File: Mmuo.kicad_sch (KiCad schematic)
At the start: 103 parts, among them IC1 A121-001-T&R, IC2 BQ24253RGER, IC3 ADPL40502AUJZ-1.8-R7, IC4 RAA2361052GNP#HC5, J1 USB_C_Receptacle_USB2.0_16P, J2 B2B-PH-K-S, J3 SW_Debug, Q1 BSS84, Q2 BSS138, Q3 MMBT3904, SW1 PTS815, U1 USBLC6-2SC6, U3 EKMB1309113K, U4 STM32WB55CGU6, U5 MCP9808_MSOP, Y1 24MHz, Y2 32MHz, Y3 32K768

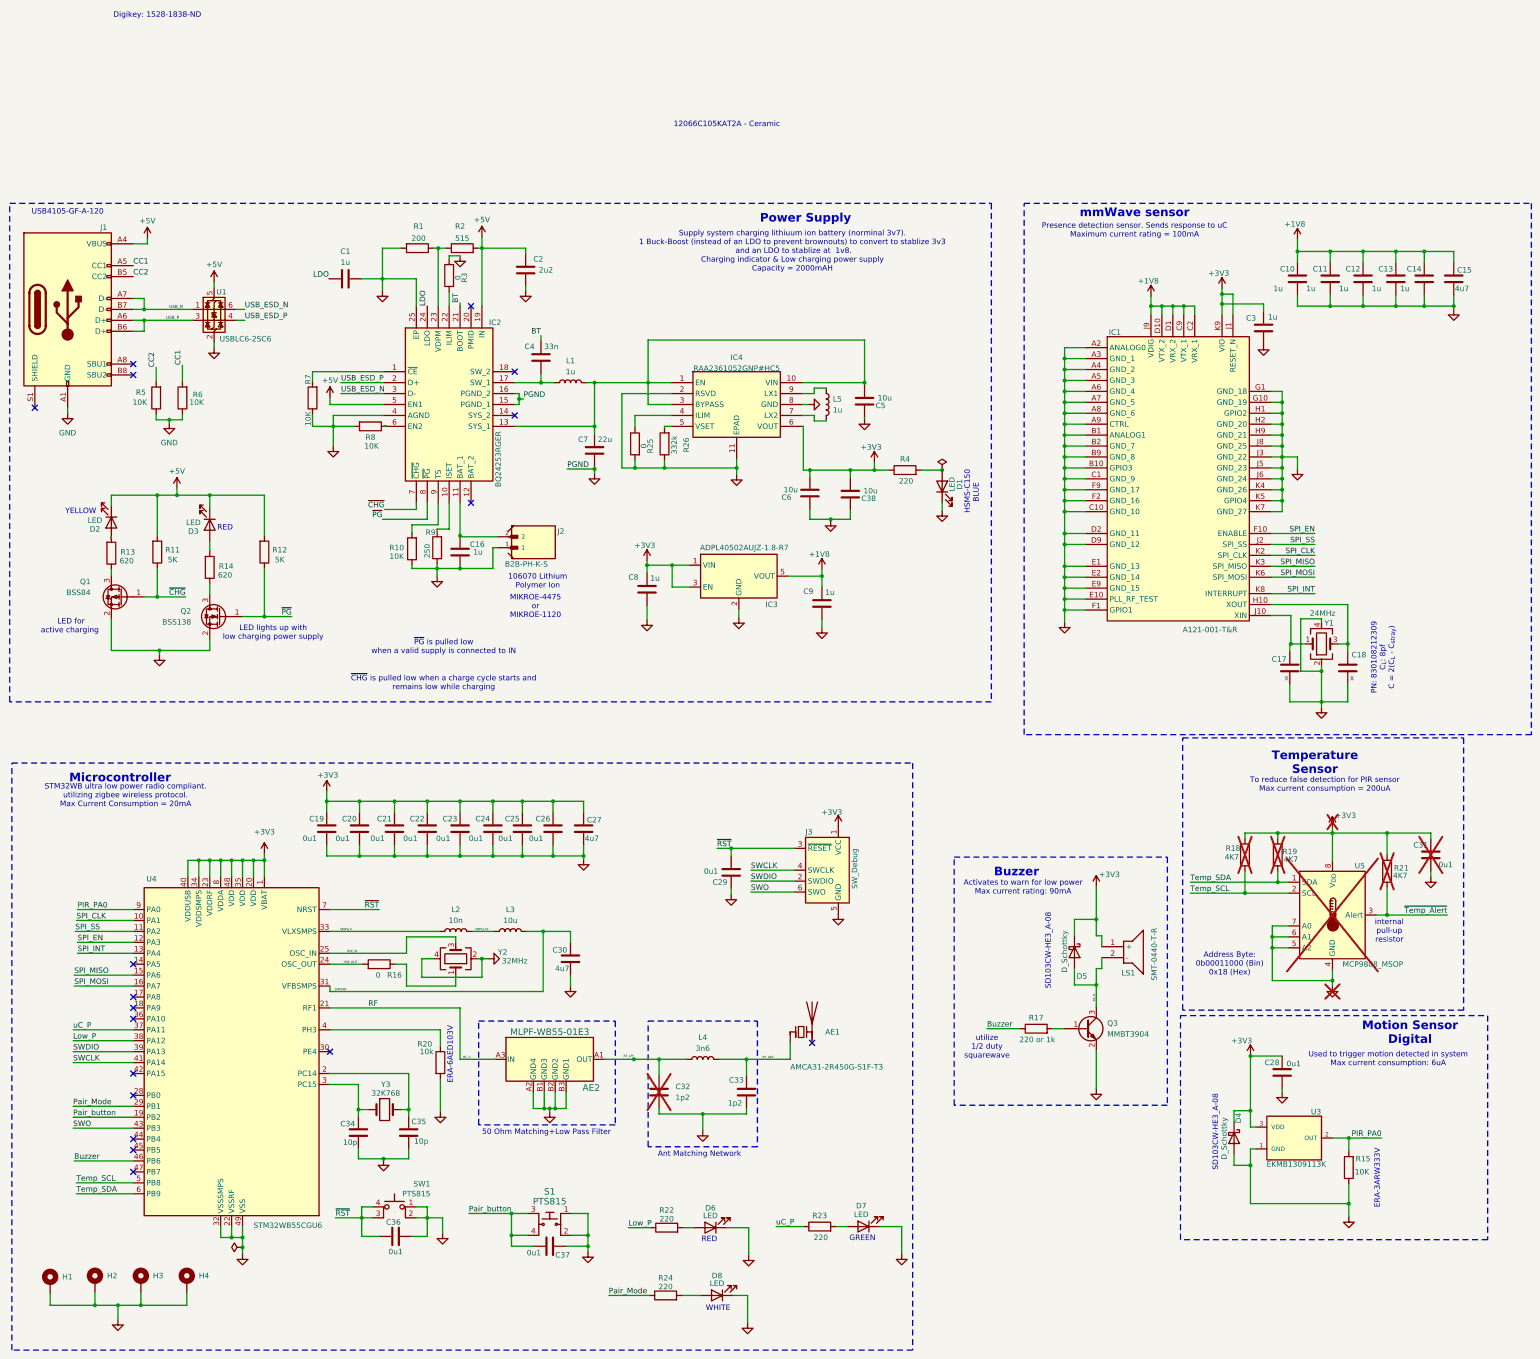
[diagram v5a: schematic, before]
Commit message: V2.0: using a TOF sensor instead of a mmWave sensor
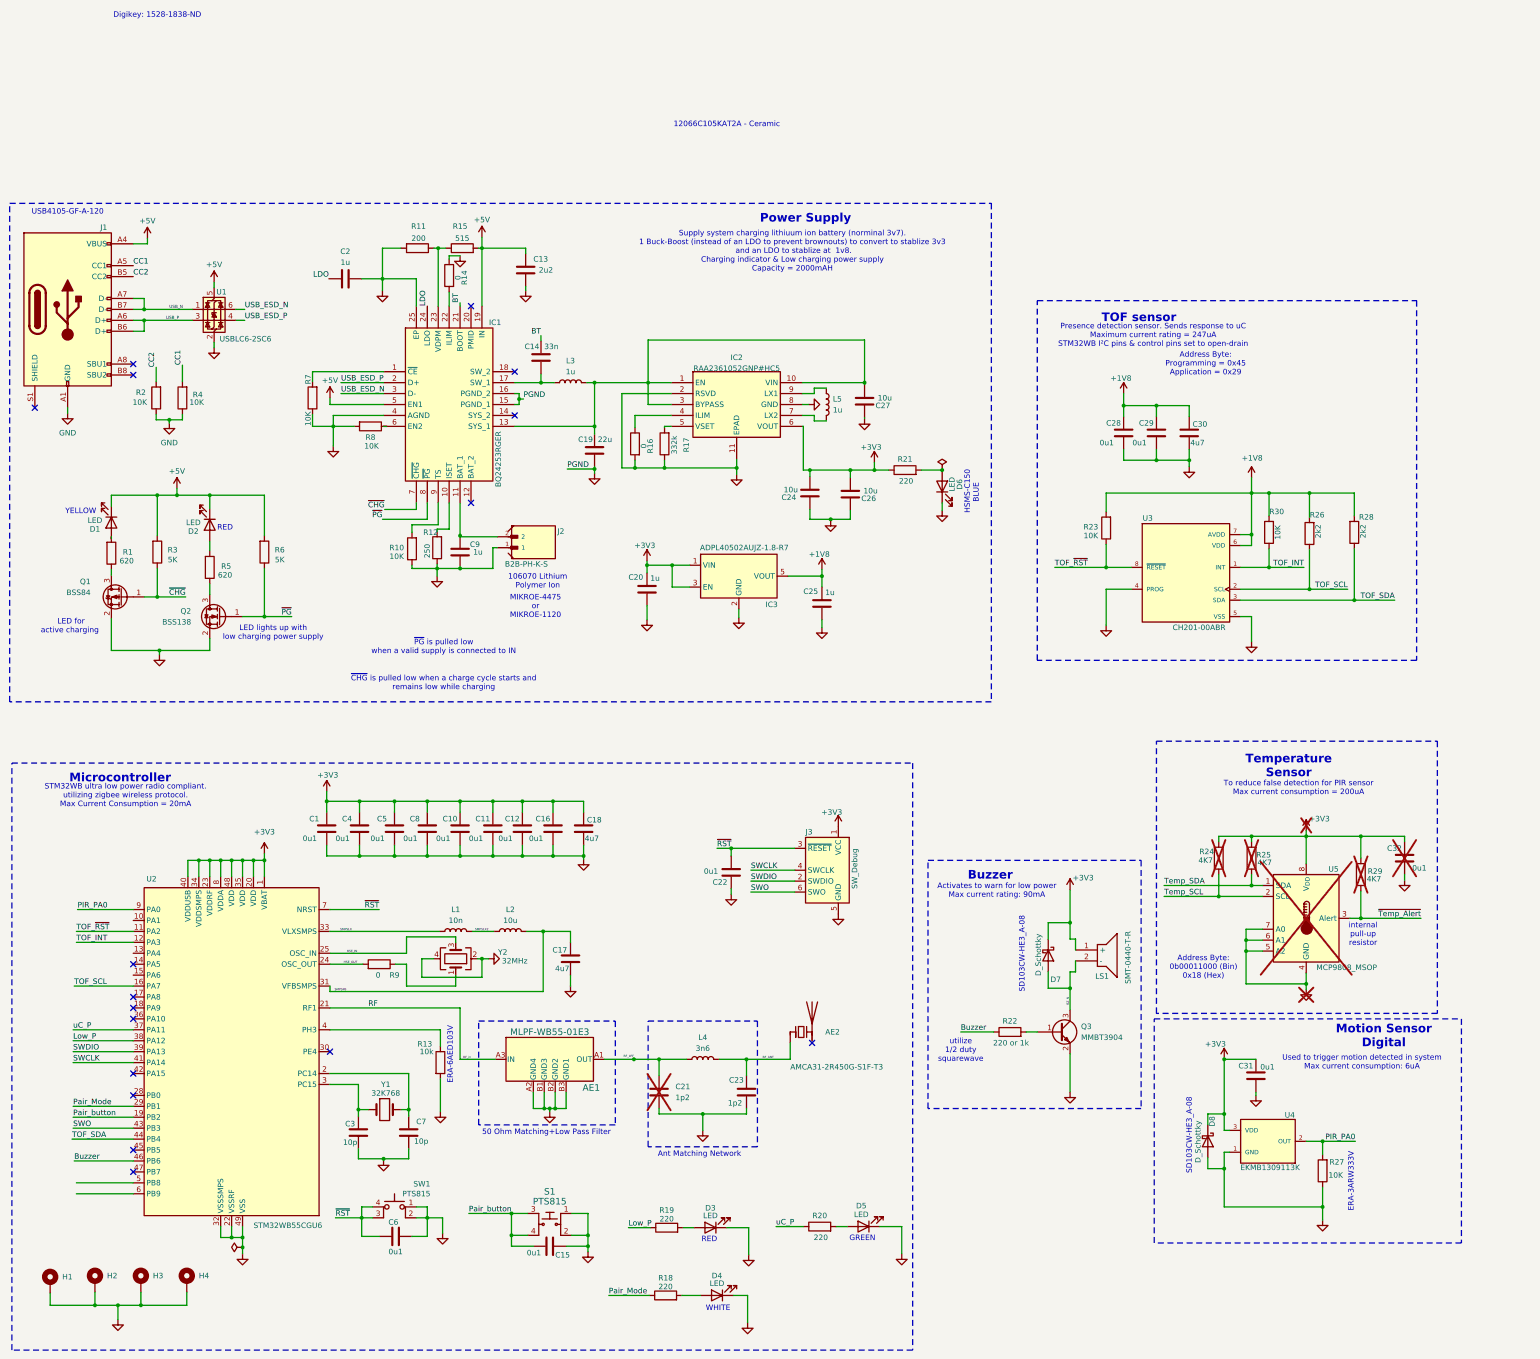
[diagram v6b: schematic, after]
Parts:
- removed C10, C11, C12, C13, C14, C3: 1u, Capacitor_SMD:C_0603_1608Metric_Pad1.08x0.95mm_HandSolder, symbol Device:C
- removed C15: 4u7, Capacitor_SMD:C_0805_2012Metric_Pad1.18x1.45mm_HandSolder, symbol Device:C
- removed C17, C18: x, Capacitor_SMD:C_0603_1608Metric_Pad1.08x0.95mm_HandSolder, symbol Device:C
- removed IC1: A121-001-T&R, A121-001-T&R:A121001TR, symbol A121-001-T&R:A121-001-T&R
- removed Y1: 24MHz, Crystal:Crystal_SMD_2016-4Pin_2.0x1.6mm, symbol Device:Crystal_GND24
- added C28, C29: 0u1, Capacitor_SMD:C_0603_1608Metric_Pad1.08x0.95mm_HandSolder, symbol Device:C
- added C30: 4u7, Capacitor_SMD:C_0805_2012Metric_Pad1.18x1.45mm_HandSolder, symbol Device:C
- added R23, R30: 10K, Resistor_SMD:R_0603_1608Metric_Pad0.98x0.95mm_HandSolder, symbol Device:R
- added R26, R28: 2k2, Resistor_SMD:R_0603_1608Metric_Pad0.98x0.95mm_HandSolder, symbol Device:R
- added U3: CH201-00ABR, CH201-00ABR:XDCR_CH201-00ABR, symbol CH201-00ABR:CH201-00ABR
- H1, H2, H3, H4: footprint MountingHole:MountingHole_3.2mm_M3_DIN965_Pad_TopBottom -> MountingHole:MountingHole_3.5mm_Pad_TopBottom
- renumbered AE2 to AE1, AE1 to AE2, C19 to C1, C23 to C10, C24 to C11, C25 to C12, C2 to C13, C4 to C14, C37 to C15, C26 to C16, C30 to C17, C27 to C18, C7 to C19, C1 to C2, C8 to C20, C32 to C21, C29 to C22, C33 to C23, C6 to C24, C9 to C25, C38 to C26, C5 to C27, C34 to C3, C28 to C31, C31 to C32, C20 to C4, C21 to C5, C36 to C6, C35 to C7, C22 to C8, C16 to C9, D2 to D1, D3 to D2, D6 to D3, D8 to D4, D7 to D5, D1 to D6, D5 to D7, D4 to D8, IC2 to IC1, IC4 to IC2, L2 to L1, L3 to L2, L1 to L3, R13 to R1, R1 to R11, R9 to R12, R20 to R13, R3 to R14, R2 to R15, R25 to R16, R26 to R17, R24 to R18, R22 to R19, R5 to R2, R23 to R20, R4 to R21, R17 to R22, R18 to R24, R19 to R25, R15 to R27, R21 to R29, R11 to R3, R6 to R4, R14 to R5, R12 to R6, R16 to R9, U4 to U2, U3 to U4, Y3 to Y1
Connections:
- net +1V8: now also C28.1, C29.1, C30.1, R23.2, R26.2, R28.2, R30.2, U3.6 (VDD), U3.7 (AVDD)
- net GND: now also C28.2, C29.2, C30.2, U3.4 (PROG), U3.5 (VSS)
- net Temp_SCL: no longer U2.5 (PB8)
- net Temp_SDA: no longer U2.6 (PB9)
- net TOF_SDA: now reaches U2.44 (PB4)
- net TOF_SDA: now also R28.1, U3.3 (SDA)
- net SPI_CLK: no longer names the net of U2.10 (PA1)
- net SPI_EN renamed TOF_INT
- net TOF_INT: now also R30.1, U3.1 (INT)
- net SPI_INT: no longer names the net of U2.13 (PA4)
- net SPI_MISO: no longer names the net of U2.15 (PA6)
- net SPI_MOSI renamed TOF_SCL
- net TOF_SCL: now also R26.1, U3.2 (SCL)
- net SPI_SS renamed TOF_~{RST}
- net TOF_~{RST}: now also R23.1, U3.8 (~{RESET})
- no-connect marks 18 -> 17
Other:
- note added: "Address Byte: Programming = 0x45 Application = 0x29"
- note added: "Presence detection sensor. Sends response to uC Maximum current rating = 247uA STM32WB I²C pins & control pins set to open-drain"
- note added: "TOF sensor"
- note removed: "PN: 830108212309 C_{L}: 8pf C = 2(C_{L} - C_{stray})"
- note removed: "Presence detection sensor. Sends response to uC Maximum current rating = 100mA"
- note removed: "mmWave sensor"
- moved on the sheet: C31, C32, D7, D8, LS1, Q3, R22, R24, R25, R27, R29, U4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

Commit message: 25_12_22_10
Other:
- note added: "${TITLE} ${REVISION}"
- moved on the sheet: C28, C29, C30, D7, LS1, Q3, R22, R23, R26, R28, R30, U3
